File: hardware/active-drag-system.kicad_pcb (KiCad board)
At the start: 4 copper layers, 33 x 90 mm, 102 parts, among them J1 Conn_01x02_Pin, J2 Conn_01x02_Socket, J3 10118193-0001LF, J4 Conn_01x05_Pin, J5 Conn_01x02_Pin, J6 Conn_01x02_Pin, J7 Conn_01x03_Pin, J8 Conn_01x03_Pin, SW1 PTS815 SJM 250 SMTR LFS, U1 RP2040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

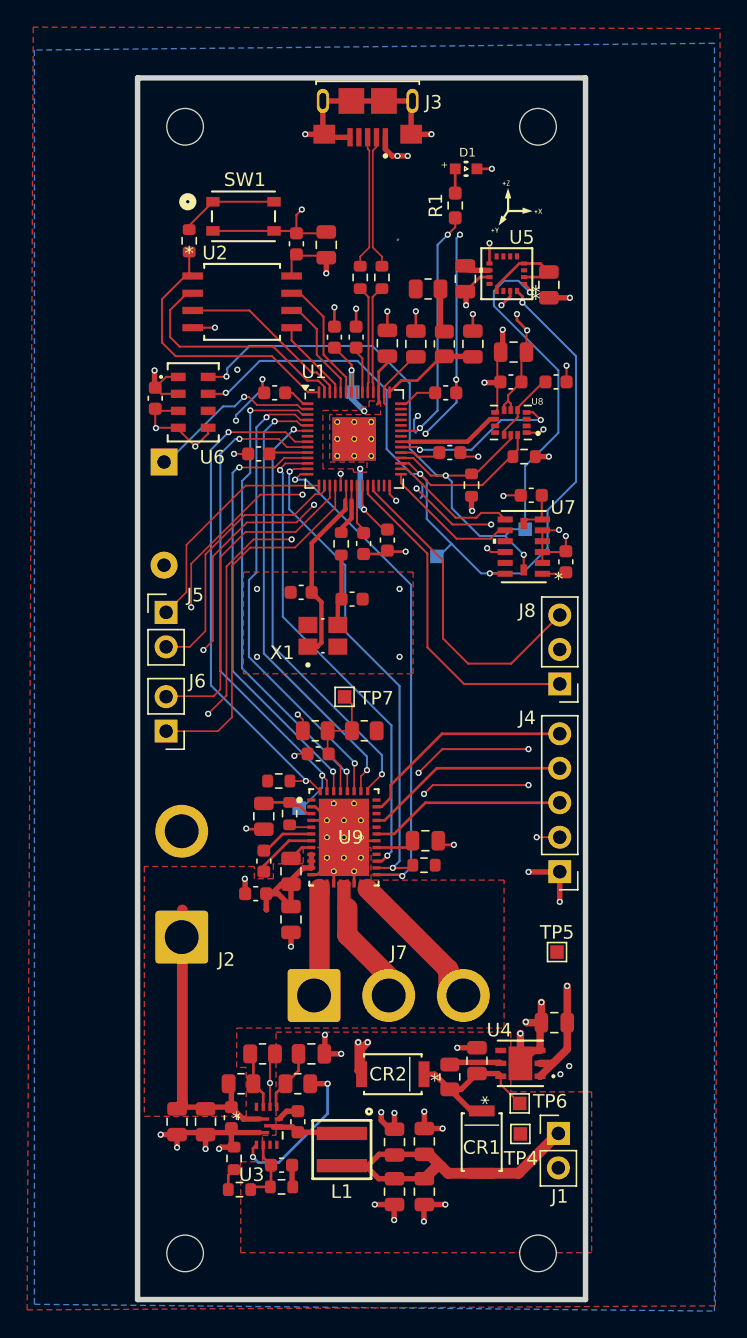
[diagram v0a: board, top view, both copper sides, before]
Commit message: swapped power order of power reg and motor driver for better / edge connections
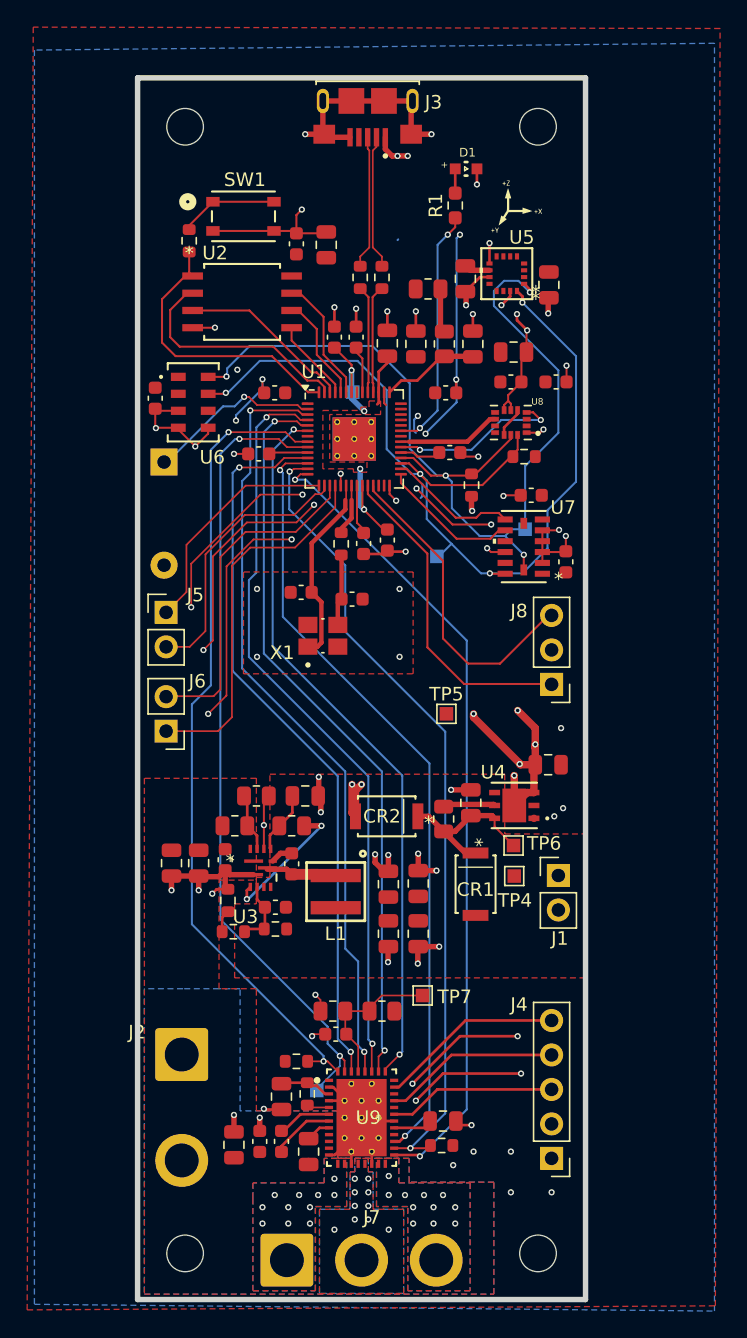
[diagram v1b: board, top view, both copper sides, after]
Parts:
- moved G*** 38.7 mm to (147.5, 101.4)
- moved TP7 22.7 mm to (152.5, 128.0)
- moved J4 21.1 mm to (162.0, 140.0)
- moved TP8 20.8 mm to (144.7, 135.0)
- moved C38 20.7 mm to (142.1, 138.8)
- moved C39 20.7 mm to (144.1, 139.5)
- moved C41 20.7 mm to (154.0, 137.2)
- moved R17 20.7 mm to (149.5, 129.2)
- moved R18 20.7 mm to (145.9, 129.2)
- moved R20 20.7 mm to (144.0, 135.2)
- moved R21 20.7 mm to (153.9, 139.1)
- moved U9 20.7 mm to (148.0, 137.0)
- moved C40 20.7 mm to (146.1, 130.8)
- moved C42 20.7 mm to (142.1, 135.4)
- moved R19 20.7 mm to (143.2, 132.8)
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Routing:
- net /+3V3: track 75.9 -> 21.8 mm, vias 12 -> 10
- net /VBAT: track 33.5 -> 0.30 mm
- net /+5V: track 24.2 -> 0.07 mm
- net /MCU_RP2040/DRVOFF: track 36.5 -> 60.0 mm
- net /MCU_RP2040/nFAULT: track 36.7 -> 59.6 mm
- net /MCU_RP2040/nSLEEP: track 35.1 -> 57.5 mm
- net /MCU_RP2040/FGOUT: track 37.8 -> 60.1 mm
- net /MCU_RP2040/SPI0_RX: track 32.1 -> 53.5 mm
- net /MCU_RP2040/MOTOR_PWM: track 38.5 -> 59.7 mm
- net /MCU_RP2040/SPI0_SCK: track 34.6 -> 55.8 mm
- net /MCU_RP2040/BRAKE: track 32.5 -> 53.7 mm
- net /MCU_RP2040/SPI0_TX: track 33.5 -> 54.7 mm
- net /MCU_RP2040/SPI0_CSn0: track 35.9 -> 57.0 mm
- net /Motor Driver/PHASE_B: track 13.5 -> 0.00 mm, vias 0 -> 10
- net /Motor Driver/PHASE_C: track 11.3 -> 0.00 mm, vias 0 -> 11
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- added copper zone on B.Cu, net /Motor Driver/PHASE_A
- added copper zone on F.Cu, net /Motor Driver/PHASE_A
- added copper zone on B.Cu, net /Motor Driver/PHASE_B
- added copper zone on F.Cu, net /Motor Driver/PHASE_B
- added copper zone on B.Cu, net /Motor Driver/PHASE_C
- added copper zone on F.Cu, net /Motor Driver/PHASE_C
- added copper zone on B.Cu, net /VBAT

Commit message: Added digikey part numbers; usb trace width update
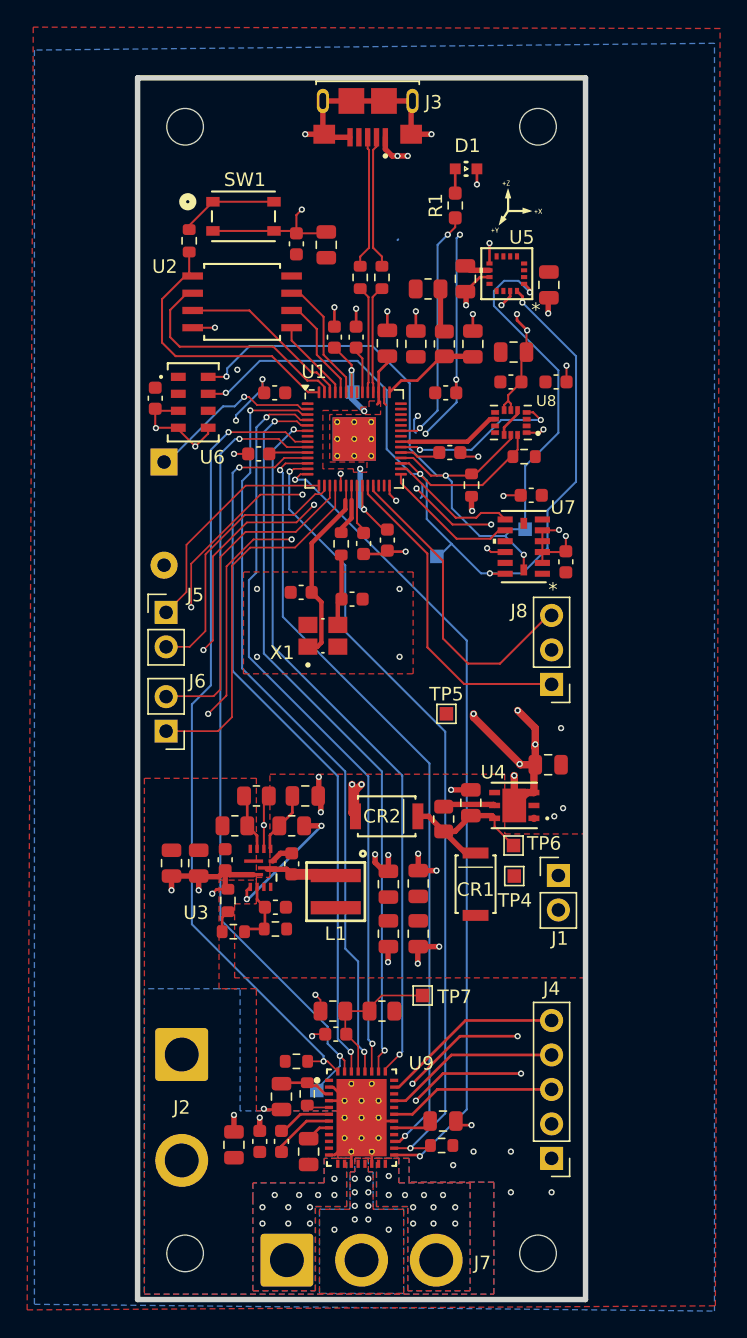
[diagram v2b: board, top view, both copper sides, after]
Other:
- board text added: "Designed by Dawsyn Schraiber Kemper Brown Cian Capacci with help from Gabe Mills"

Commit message: Minimal design (aka w/o motor driver and added GPIO out); gerbers
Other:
- board text added: "Active Drag System: Rev 1 Designed by: Dawsyn Schraiber Kemper Brown Cian Capacci with help from Gabe Mills"
- board text removed: "Designed by Dawsyn Schraiber Kemper Brown Cian Capacci with help from Gabe Mills"

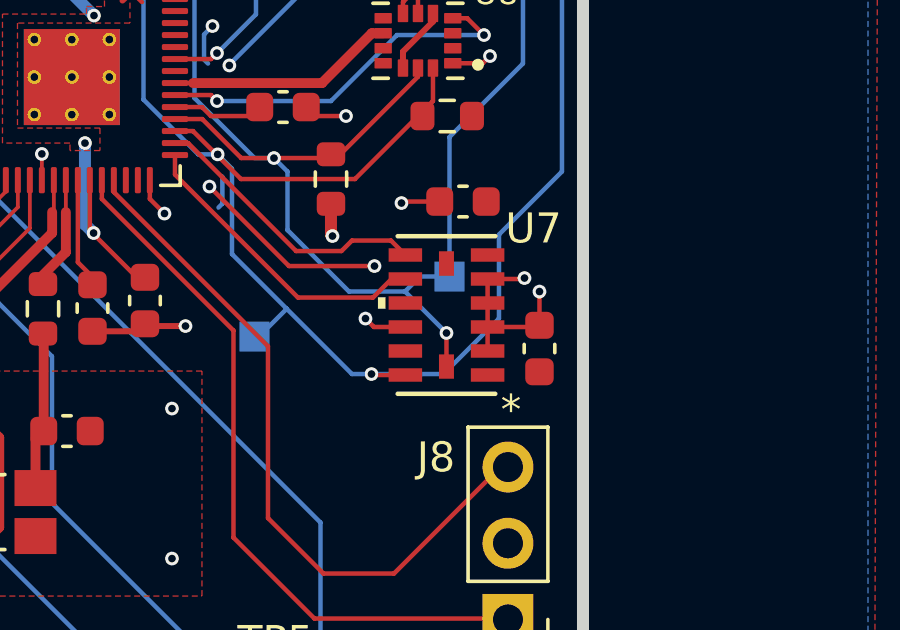
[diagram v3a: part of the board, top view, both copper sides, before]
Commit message: Removed bad GND connection to reserved pin on ADXL375 IMU; first error found in first batch
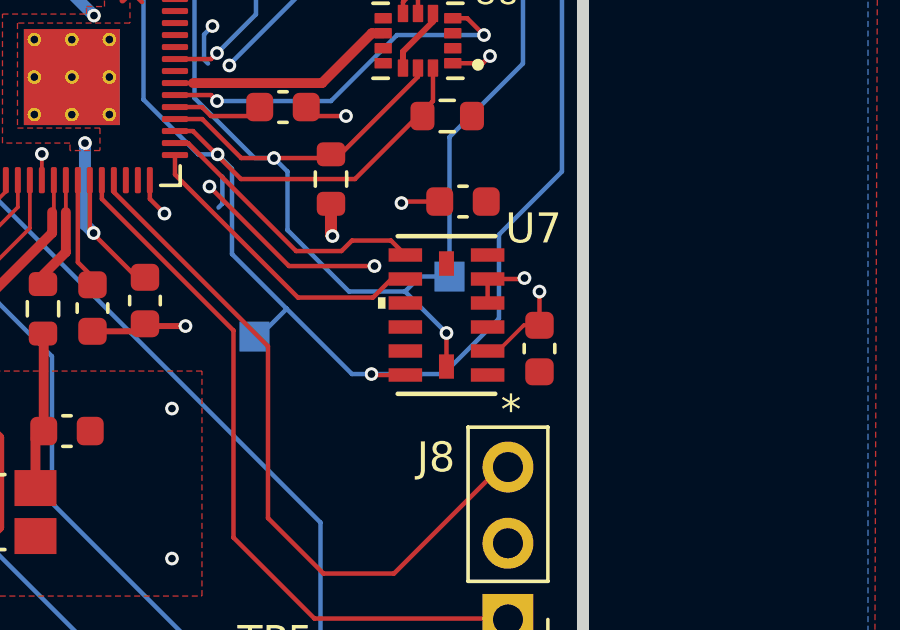
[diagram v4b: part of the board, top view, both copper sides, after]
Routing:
- net GND: track 239.1 -> 236.4 mm, vias 74 -> 73
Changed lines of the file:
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@@
+	)
+	(segment
+		(start 161.320901 96.131502)
+		(end 161.668498 96.131502)
+		(width 0.127)
+		(layer "F.Cu")
+		(net 1)
 	)
 	(segment
@@
 	)
 	(segment
+		(start 161.668498 96.131502)
+		(end 162.525 95.275)
+		(width 0.127)
+		(layer "F.Cu")
+		(net 1)
+	)
+	(segment
 		(start 149.975887 117.656175)
 		(end 149.969586 117.649874)
@@
 	)
 	(segment
-		(start 157.531501 95.331501)
-		(end 157.25 95.05)
-		(width 0.15)
-		(layer "F.Cu")
-		(net 1)
-	)
-	(segment
 		(start 144.975 128.325)
 		(end 144.975 129.15)
@@
 		(start 158.8 84.2)
 		(end 159 84.4)
-		(width 0.15)
-		(layer "F.Cu")
-		(net 1)
-	)
-	(segment
-		(start 161.320901 96.131502)
-		(end 161.320901 93.731502)
 		(width 0.15)
 		(layer "F.Cu")
@@
 	)
 	(segment
-		(start 161.320901 95.331501)
-		(end 162.993499 95.331501)
-		(width 0.15)
-		(layer "F.Cu")
-		(net 1)
-	)
-	(segment
 		(start 158.8 83.775)
 		(end 159.775 82.8)
@@
 	)
 	(segment
+		(start 161.320901 93.731502)
+		(end 161.320901 94.531503)
+		(width 0.15)
+		(layer "F.Cu")
+		(net 1)
+	)
+	(segment
 		(start 160.6978 113.049999)
 		(end 160.200001 113.049999)
@@
 	)
 	(segment
+		(start 162.525 95.275)
+		(end 163.05 95.275)
+		(width 0.127)
+		(layer "F.Cu")
+		(net 1)
+	)
+	(segment
 		(start 137.954101 119.975126)
 		(end 138.154101 120.175126)
@@
 	)
 	(segment
-		(start 158.579099 95.331501)
-		(end 157.531501 95.331501)
-		(width 0.15)
-		(layer "F.Cu")
-		(net 1)
-	)
-	(segment
 		(start 151.65 62.2)
 		(end 151.75 62.1)
@@
 		(size 0.4572)
 		(drill 0.254)
-		(layers "F.Cu" "B.Cu")
-		(free yes)
-		(net 1)
-	)
-	(via
-		(at 157.25 95.05)
-		(size 0.4572)
-		(drill 0.254)

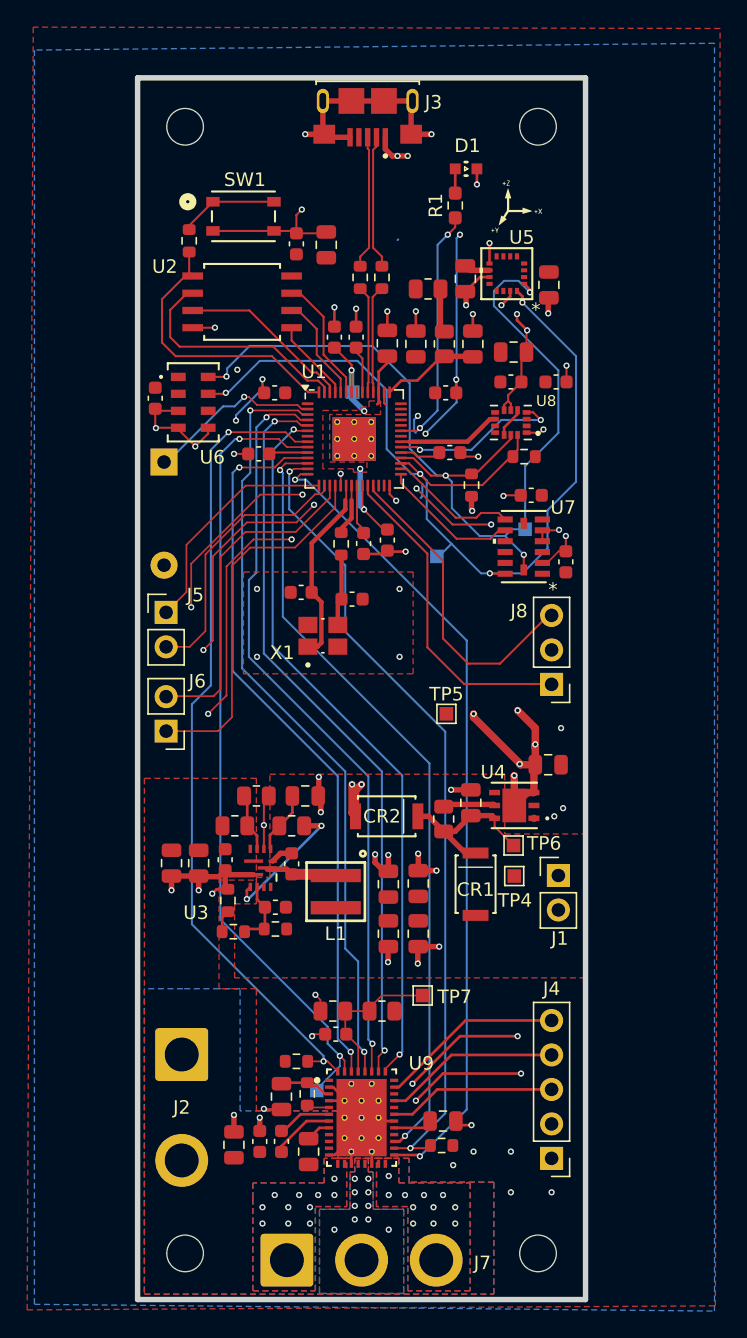
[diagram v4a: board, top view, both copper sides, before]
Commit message: Rev 2 of Custom PCB but without Motor Driver (Replaced with Optocoupler Circuit for Standard Servo) (#15)
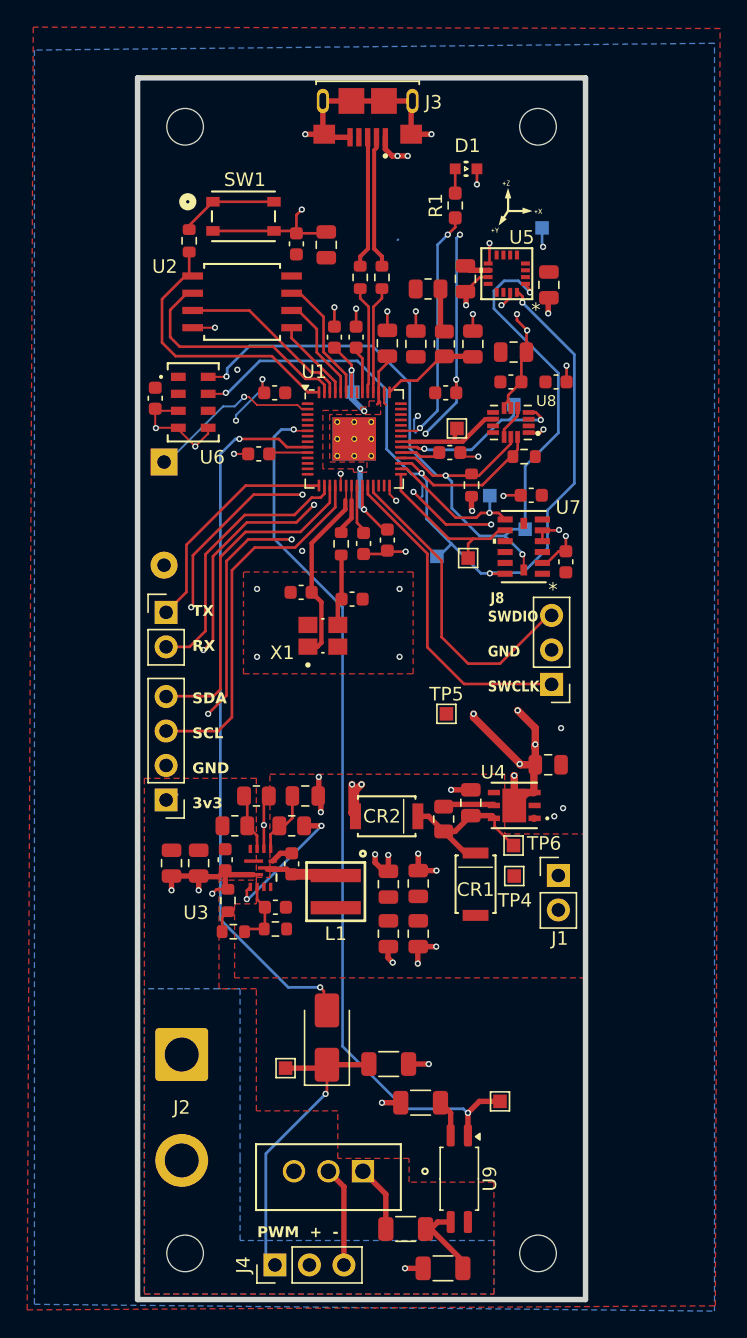
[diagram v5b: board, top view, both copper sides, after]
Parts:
- removed C36, C40: 100nF, Capacitor_SMD:C_0603_1608Metric
- removed C37: 10uF, Capacitor_SMD:C_0805_2012Metric
- removed C38: 47nF, Capacitor_SMD:C_0603_1608Metric
- removed C39, C41: 1uF, Capacitor_SMD:C_0805_2012Metric
- removed C42: 22uF, Capacitor_SMD:C_0805_2012Metric
- removed J7: Conn_01x03_Pin, active-drag-system:SolderWire-2sqmm_1x03_P7.8mm_D2mm_OD3.9mm
- removed R21: 10k, Resistor_SMD:R_0603_1608Metric
- added D2: S1G, Diode_SMD:D_SMA, F.Cu at (145.4, 131.1)
- added TP17: CLKIN, TestPoint:TestPoint_Pad_1.0x1.0mm, F.Cu at (155.0, 86.2)
- added TP18: MGINT, TestPoint:TestPoint_Pad_1.0x1.0mm, B.Cu at (159.2, 84.5)
- added TP19: MINT, TestPoint:TestPoint_Pad_1.0x1.0mm, B.Cu at (161.3, 71.5)
- added TP20: HGINT1, TestPoint:TestPoint_Pad_1.0x1.0mm, B.Cu at (157.4, 91.2)
- added TP21: HGINT2, TestPoint:TestPoint_Pad_1.0x1.0mm, F.Cu at (155.8, 95.8)
- added U10: STP55NF06, active-drag-system:STP55NF06, F.Cu at (148.1, 140.9)
- J4: value Conn_01x05_Pin -> Conn_01x03_Pin; footprint Connector_PinHeader_2.54mm:PinHeader_1x05_P2.54mm_Vertical -> Connector_PinHeader_2.54mm:PinHeader_1x03_P2.54mm_Vertical
- J6: value Conn_01x02_Pin -> Conn_01x04_Pin; footprint Connector_PinHeader_2.54mm:PinHeader_1x02_P2.54mm_Vertical -> Connector_PinHeader_2.54mm:PinHeader_1x04_P2.54mm_Vertical
- R17: value 164k -> 4.7k; footprint Resistor_SMD:R_0805_2012Metric -> Resistor_SMD:R_1206_3216Metric
- R18: value 100k -> 4.7k; footprint Resistor_SMD:R_0805_2012Metric -> Resistor_SMD:R_1206_3216Metric
- R19: value 10k -> 1k; footprint Resistor_SMD:R_0603_1608Metric -> Resistor_SMD:R_1206_3216Metric
- R20: value 22 -> 220; footprint Resistor_SMD:R_0603_1608Metric -> Resistor_SMD:R_1206_3216Metric
- TP7: value ILIM -> SERVO_ENABLE
- TP8: value PWM -> SERVO_PWM; moved to F.Cu
- U9: value MCT8316Z0RRGFR -> FODM217A; footprint active-drag-system:RGF0040E-MFG -> Package_SO:SOP-4_4.4x2.6mm_P1.27mm
- moved J4 21.8 mm to (141.6, 147.8), turned to 90 degrees
- moved R18 20.6 mm to (154.0, 148.1)
- moved R19 14.7 mm to (151.2, 145.2)
- moved TP7 9.66 mm to (158.2, 135.8)
- moved U9 8.49 mm to (155.2, 141.5), turned to -90 degrees
- moved R20 8.38 mm to (152.3, 135.9), turned to 0 degrees
- moved J6 5.07 mm to (133.6, 113.6)
- moved R17 3.93 mm to (150.0, 133.1), turned to 180 degrees
- moved TP8 2.83 mm to (142.4, 133.3), turned to 0 degrees
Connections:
- J4 pad 1: /+3V3 -> Net-(D2-K)
- J4 pad 2: GND -> /VBAT
- J4 pad 3: /Motor Driver/HALL_SENSE_A -> Net-(J4-Pin_3)
- J6 pad 1: /MCU_RP2040/I2C1_SCL -> /+3V3
- J6 pad 2: /MCU_RP2040/I2C1_SDA -> GND
- R17 pad 1: Net-(U9-ILIM) -> GND
- R17 pad 2: /+3V3 -> Net-(D2-K)
- R18 pad 1: Net-(U9-ILIM) -> Net-(R18-Pad1)
- R19 pad 1: /+3V3 -> Net-(R19-Pad1)
- R19 pad 2: /MCU_RP2040/FGOUT -> Net-(R18-Pad1)
- R20 pad 1: Net-(U9-SW_BK) -> GND
- R20 pad 2: Net-(U9-FB_BK) -> Net-(R20-Pad2)
- TP7 pad 1: Net-(U9-ILIM) -> /MCU_RP2040/SERVO_ENABLE
- TP8 pad 1: /MCU_RP2040/MOTOR_PWM -> Net-(D2-K)
- U1 pad 11: /MCU_RP2040/BRAKE -> unconnected-(U1-GPIO8-Pad11)
- U1 pad 12: /MCU_RP2040/nSLEEP -> unconnected-(U1-GPIO9-Pad12)
- U1 pad 13: /MCU_RP2040/nFAULT -> unconnected-(U1-GPIO10-Pad13)
- U1 pad 14: /MCU_RP2040/DRVOFF -> unconnected-(U1-GPIO11-Pad14)
- U1 pad 3: /MCU_RP2040/SPI0_CSn0 -> unconnected-(U1-GPIO1-Pad3)
- U1 pad 4: /MCU_RP2040/SPI0_SCK -> unconnected-(U1-GPIO2-Pad4)
- U1 pad 5: /MCU_RP2040/SPI0_TX -> unconnected-(U1-GPIO3-Pad5)
- U1 pad 6: /MCU_RP2040/SPI0_RX -> /MCU_RP2040/SERVO_ENABLE
- U1 pad 8: /MCU_RP2040/FGOUT -> unconnected-(U1-GPIO6-Pad8)
- U7 pad 11: GND -> unconnected-(U7-RESERVED-Pad11)
- U7 pad 3: GND -> unconnected-(U7-RESERVED-Pad3)
- U9 pad 1: unconnected-(U9-NC-Pad1) -> /MCU_RP2040/SERVO_ENABLE
- U9 pad 2: GND -> Net-(R20-Pad2)
- U9 pad 3: Net-(U9-FB_BK) -> Net-(R18-Pad1)
- U9 pad 4: GND -> /VBAT
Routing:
- net /MCU_RP2040/SERVO_ENABLE: track 0.00 -> 65.4 mm, vias 0 -> 2
- net /MCU_RP2040/FGOUT: track 60.1 -> 0.00 mm, vias 2 -> 0
- net /MCU_RP2040/DRVOFF: track 60.0 -> 0.00 mm, vias 2 -> 0
- net /MCU_RP2040/nFAULT: track 59.6 -> 0.00 mm, vias 2 -> 0
- net /MCU_RP2040/nSLEEP: track 57.5 -> 0.00 mm, vias 2 -> 0
- net /MCU_RP2040/SPI0_CSn0: track 57.0 -> 0.00 mm, vias 2 -> 0
- net /MCU_RP2040/SPI0_SCK: track 55.8 -> 0.00 mm, vias 2 -> 0
- net /MCU_RP2040/SPI0_TX: track 54.7 -> 0.00 mm, vias 2 -> 0
- net /MCU_RP2040/BRAKE: track 53.7 -> 0.00 mm, vias 2 -> 0
- net /MCU_RP2040/SPI0_RX: track 53.5 -> 0.00 mm, vias 2 -> 0
- net GND: track 236.4 -> 201.6 mm, vias 73 -> 67
- net Net-(D2-K): track 0.00 -> 23.2 mm, vias 0 -> 1
- net /Motor Driver/HALL_SENSE_C: track 13.6 -> 0.00 mm
- net /Motor Driver/HALL_SENSE_B: track 13.0 -> 0.00 mm
- net /Motor Driver/HALL_SENSE_A: track 12.4 -> 0.00 mm
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- removed copper zone on B.Cu, net /Motor Driver/PHASE_A
- removed copper zone on F.Cu, net /Motor Driver/PHASE_A
- removed copper zone on B.Cu, net /Motor Driver/PHASE_B
- removed copper zone on F.Cu, net /Motor Driver/PHASE_B
- removed copper zone on B.Cu, net /Motor Driver/PHASE_C
- removed copper zone on F.Cu, net /Motor Driver/PHASE_C
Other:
- board text added: "Active Drag System: Rev 2 (Backup) Designed by: Dawsyn Schraiber Kemper Brown Cian Capacci with help from Gabe Mills"
- board text added: "PWM + -"
- board text added: "SWDIO GND SWCLK"
- board text added: "TX RX SDA SCL GND 3v3"
- board text removed: "Active Drag System: Rev 1 Designed by: Dawsyn Schraiber Kemper Brown Cian Capacci with help from Gabe Mills"
